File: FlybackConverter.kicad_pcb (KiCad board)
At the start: 2 copper layers, 76.2 x 76.2 mm, 42 parts, among them J1 USB_C_Receptacle_PowerOnly_6P, T1 Transformer_1P_2S, U1 LNK6428K, U2 TPS25820DSST

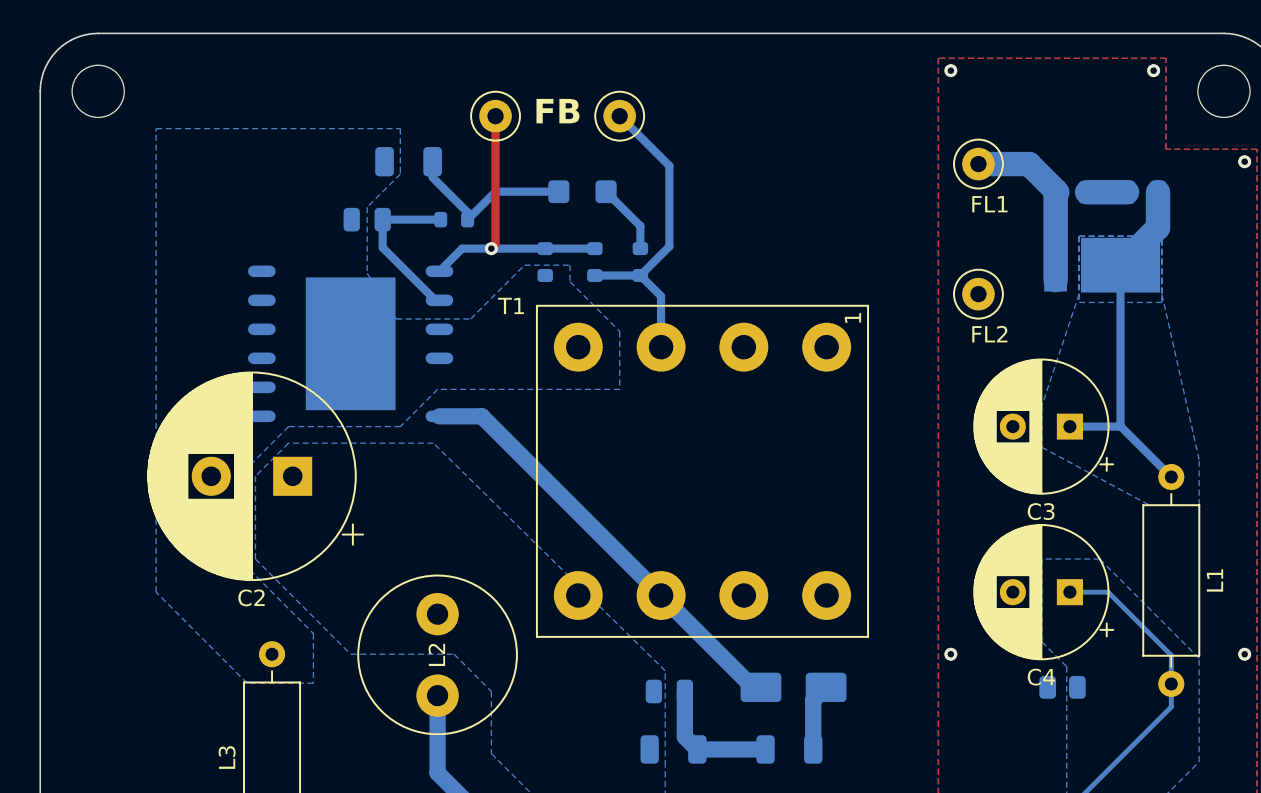
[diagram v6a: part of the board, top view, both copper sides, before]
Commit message: トランスのフットプリントを10pinに修正
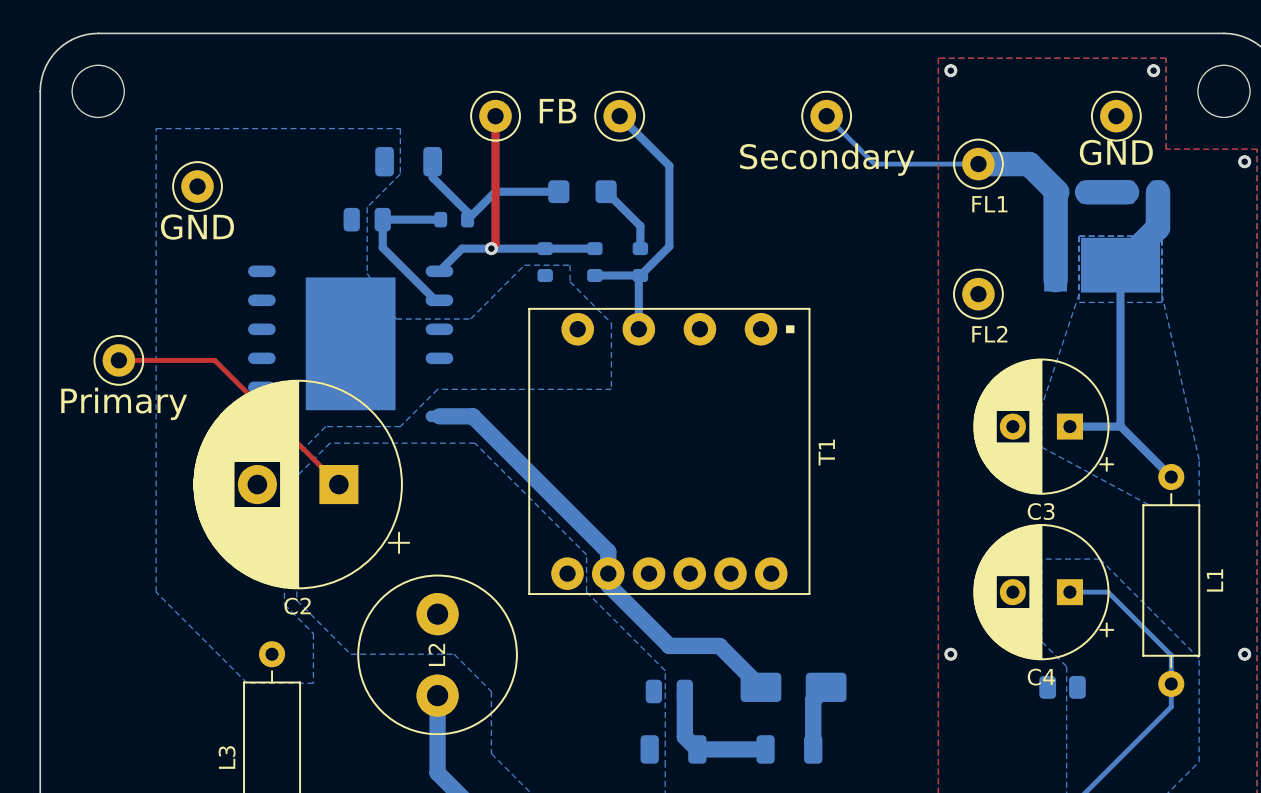
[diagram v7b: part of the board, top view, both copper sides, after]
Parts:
- added TP5: TestPoint, TestPoint:TestPoint_Loop_D1.80mm_Drill1.0mm_Beaded, F.Cu at (175.3, 55.9)
- added TP6: TestPoint, TestPoint:TestPoint_Loop_D1.80mm_Drill1.0mm_Beaded, F.Cu at (193.0, 55.9)
- added TP7: Primary, TestPoint:TestPoint_Loop_D1.80mm_Drill1.0mm_Beaded, F.Cu at (131.8, 70.9)
- added TP8: GND, TestPoint:TestPoint_Loop_D1.80mm_Drill1.0mm_Beaded, F.Cu at (136.7, 60.2)
- T1: footprint Transformer_THT:Transformer_CHK_EI38-3VA_2xSec -> 00_Library:BEPC17-1110CPHFR
- moved T1 16.9 mm to (165.6, 76.5)
- moved C2 2.88 mm to (145.3, 78.5)
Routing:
- net Net-(T1-AA): track 0.00 -> 16.7 mm
- net FL1: track 10.9 -> 21.4 mm
- net Net-(T1-SA): track 19.5 -> 17.9 mm
- net Net-(D2-A): track 26.6 -> 27.8 mm
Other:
- board text added: "GND"
- board text added: "Primary"
- board text added: "Secondary"

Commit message: TP追加 fix #3
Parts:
- moved FL2 0.13 mm to (184.5, 66.7)
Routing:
- net FL2: vias 12 -> 14
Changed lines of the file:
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@@
   )
   (footprint "TestPoint:TestPoint_Loop_D1.80mm_Drill1.0mm_Beaded" (layer "F.Cu")
-    (at 184.576 66.802)
+    (at 184.531 66.675)
     (descr "wire loop with bead as test point, loop diameter 1.8mm, hole diameter 1.0mm")
     (tags "test point wire loop bead")
@@
   (via (at 192.532 104.14) (size 0.8) (drill 0.4) (layers "F.Cu" "B.Cu") (net 18))
   (via (at 182.88 88.9) (size 0.8) (drill 0.4) (layers "F.Cu" "B.Cu") (free) (net 18))
+  (via (at 184.531 68.961) (size 0.8) (drill 0.4) (layers "F.Cu" "B.Cu") (free) (net 18))
   (via (at 182.88 118.618) (size 0.8) (drill 0.4) (layers "F.Cu" "B.Cu") (free) (net 18))
   (via (at 194.056 104.14) (size 0.8) (drill 0.4) (layers "F.Cu" "B.Cu") (free) (net 18))
   (via (at 195.326 53.086) (size 0.8) (drill 0.4) (layers "F.Cu" "B.Cu") (free) (net 18))
+  (via (at 184.531 64.389) (size 0.8) (drill 0.4) (layers "F.Cu" "B.Cu") (free) (net 18))
   (segment (start 188.79 100.84) (end 188.788 100.838) (width 0.5) (layer "B.Cu") (net 18))
   (segment (start 192.532 104.14) (end 194.056 104.14) (width 0.5) (layer "B.Cu") (net 18))
@@
   (segment (start 188.79 103.335949) (end 188.79 100.84) (width 0.5) (layer "B.Cu") (net 18))
   (segment (start 189.594051 104.14) (end 191.262 104.14) (width 0.5) (layer "B.Cu") (net 18))
-  (segment (start 184.576 58.819) (end 178.199 58.819) (width 0.3) (layer "B.Cu") (net 19))
-  (segment (start 178.199 58.819) (end 175.26 55.88) (width 0.3) (layer "B.Cu") (net 19))
   (segment (start 187.6865 58.819) (end 189.4155 60.548) (width 1.5) (layer "B.Cu") (net 19))
+  (segment (start 178.199 58.819) (end 175.26 55.88) (width 0.3) (layer "B.Cu") (net 19))
   (segment (start 184.576 58.819) (end 187.6865 58.819) (width 1.5) (layer "B.Cu") (net 19))
+  (segment (start 184.576 58.819) (end 178.199 58.819) (width 0.3) (layer "B.Cu") (net 19))
   (segment (start 189.312 60.597) (end 189.312 65.944) (width 1.5) (layer "B.Cu") (net 19))
   (segment (start 163.733 65.755) (end 163.733 68.954) (width 0.5) (layer "B.Cu") (net 20))
